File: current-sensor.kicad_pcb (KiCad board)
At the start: 2 copper layers, 78 x 39.3 mm, 34 parts, among them J1 ‎0197134001‎, J2 ‎0197134001‎, J3 0731000105, J4 Molex_SL_01x02_Male, J5 Molex_SL_01x02_Male, SW1 PN12Sxxx03QE, SW2 OS103011MA7QP1, SW3 OS103011MA7QP1, U1 ACS730xLCTR-20AB, U2 AD8616xRM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

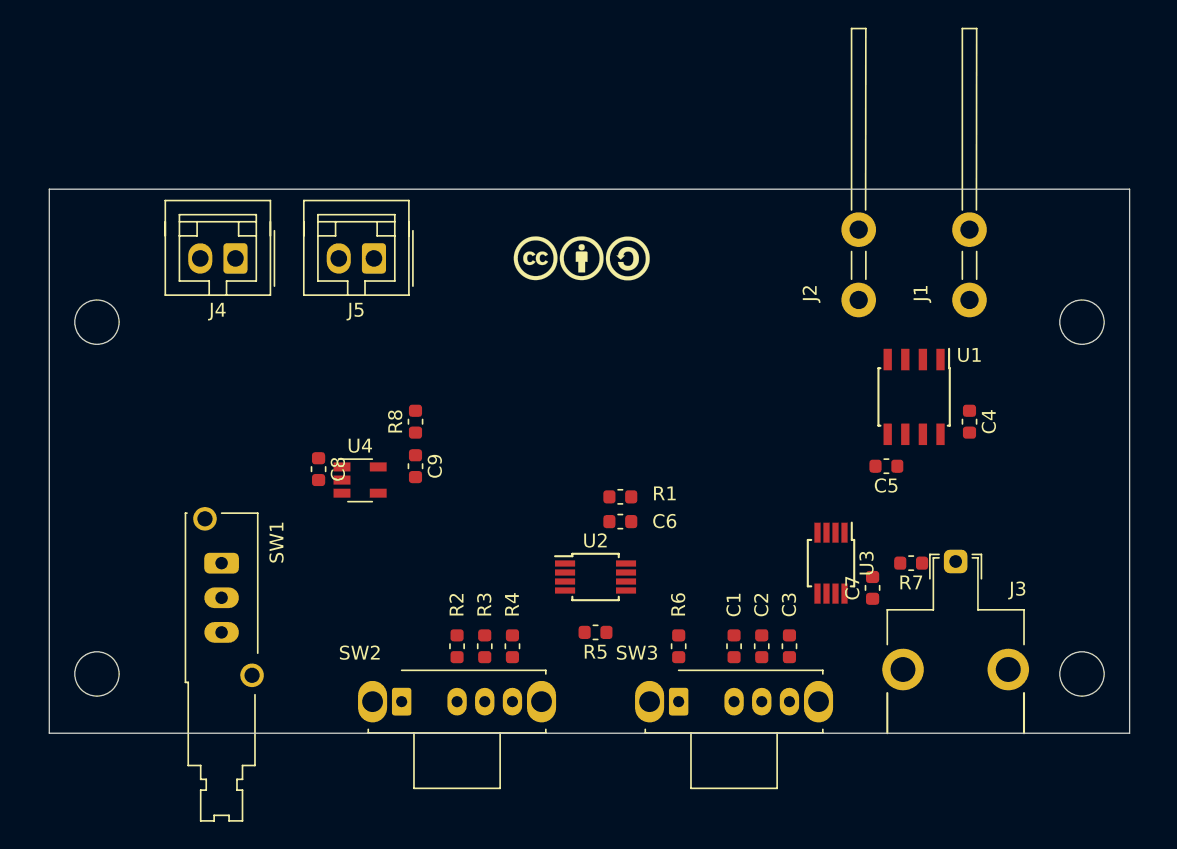
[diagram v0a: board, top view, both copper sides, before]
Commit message: complete mechanical placement of all components on main pcb, and holes on front/back panels
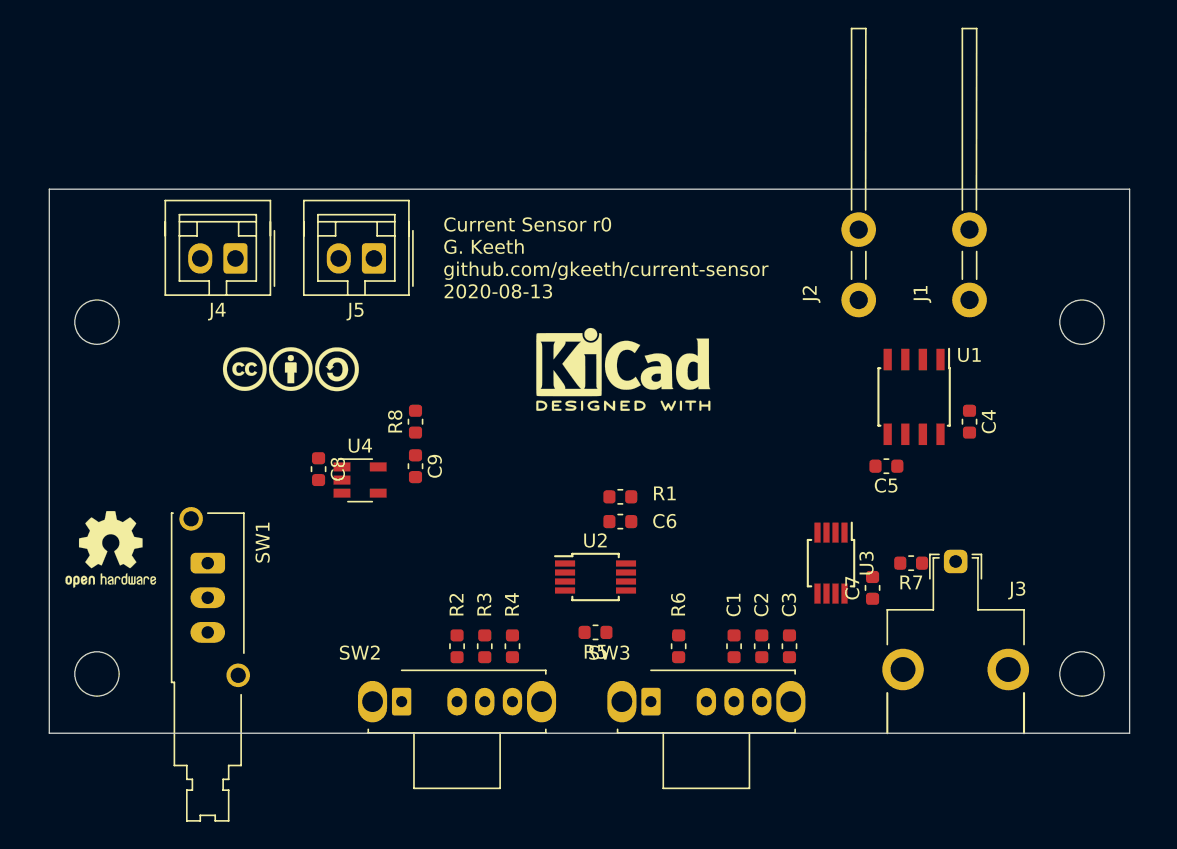
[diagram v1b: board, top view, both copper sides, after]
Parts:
- added LOGO2: Logo_MadeWithKiCad, Symbol:KiCad-Logo2_6mm_SilkScreen, F.Cu at (138.0, 78.0)
- added LOGO3: Logo_Open_Hardware_Small, Symbol:OSHW-Logo2_7.3x6mm_SilkScreen, F.Cu at (101.0, 91.0)
- U1: value ACS730xLCTR-20AB -> ACS730xLCTR-40AB
- moved LOGO1 22.5 mm to (114.0, 78.0)
- moved SW3 2.00 mm to (140.0, 102.0)
- moved SW1 1.00 mm to (108.0, 92.0)
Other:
- board text added: "Current Sensor r0 G. Keeth github.com/gkeeth/current-sensor 2020-08-13"

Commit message: complete basic schematic & routing
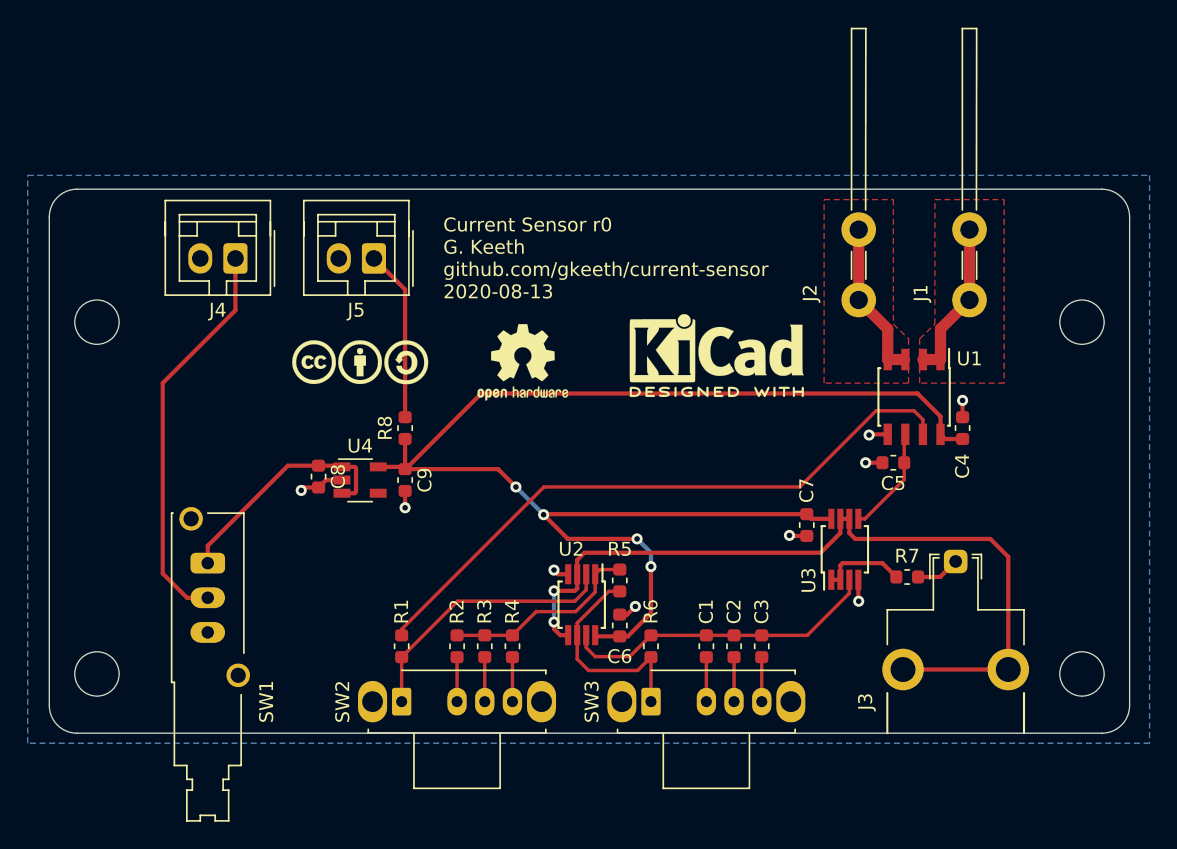
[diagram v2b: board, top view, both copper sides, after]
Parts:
- SW1: value PN12Sxxx03QE -> PN12SHNA03QE
- moved LOGO3 32.7 mm to (130.8, 77.5)
- moved R1 19.1 mm to (122.0, 98.0), turned to 270 degrees
- moved C6 7.50 mm to (137.8, 96.5), turned to 90 degrees
- moved LOGO2 6.82 mm to (144.8, 77.0)
- moved C7 6.57 mm to (151.2, 89.2), turned to 270 degrees
- moved LOGO1 5.02 mm to (119.0, 77.5)
- moved R5 4.14 mm to (137.8, 93.2), turned to 90 degrees
- moved U2 2.24 mm to (135.0, 95.0), turned to 270 degrees
- moved C1 2.00 mm to (144.0, 98.0)
- moved C2 2.00 mm to (146.0, 98.0)
- moved C3 2.00 mm to (148.0, 98.0)
- moved R6 2.00 mm to (140.0, 98.0)
- moved U3 1.41 mm to (154.0, 91.0), turned to 90 degrees
- moved C9 1.25 mm to (122.2, 86.0)
- moved R7 1.04 mm to (158.5, 93.0)
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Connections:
- net Net-(C8-Pad1) renamed /9V_switched
- net Net-(J1-Pad1) renamed /current+
- net Net-(J2-Pad1) renamed /current-
- net Net-(J3-Pad1) renamed /vout
- net Net-(J3-Pad2) renamed /virtual_gnd
- net Net-(J4-Pad1) renamed /9V
- net Net-(J5-Pad1) renamed /led_high
- R6 pad 1: Net-(C1-Pad1) -> Net-(R5-Pad1)
- R6 pad 2: Net-(R5-Pad1) -> Net-(C1-Pad1)
- SW2 pad 1: Net-(R1-Pad1) -> Net-(R1-Pad2)
- U1 pad 7: Net-(R1-Pad2) -> Net-(R1-Pad1)
- U2 pad 2: Net-(R1-Pad1) -> Net-(R1-Pad2)
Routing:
- net +5V: track 0.00 -> 99.2 mm, vias 0 -> 4
- net /virtual_gnd: track 0.00 -> 58.2 mm, vias 0 -> 2
- net Net-(R1-Pad1): track 0.00 -> 45.9 mm
- net /9V: track 0.00 -> 28.9 mm
- net Net-(C1-Pad1): track 0.00 -> 23.0 mm
- net Net-(R1-Pad2): track 0.00 -> 19.7 mm
- net /9V_switched: track 0.00 -> 17.2 mm
- net Net-(R5-Pad1): track 0.00 -> 15.9 mm
- net Net-(R2-Pad1): track 0.00 -> 14.5 mm
- net GND: track 0.00 -> 13.6 mm, vias 0 -> 9
- net /led_high: track 0.00 -> 12.4 mm
- net /current+: track 0.00 -> 11.5 mm
- net /current-: track 0.00 -> 11.5 mm
- net Net-(C5-Pad1): track 0.00 -> 7.78 mm
- net Net-(R7-Pad2): track 0.00 -> 6.20 mm
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- added copper zone on F.Cu, net /current+
- added copper zone on F.Cu, net /current-
- added copper zone on B.Cu, net GND
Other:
- outline, holes or cut-outs redrawn
- net class analog added: clearance 0.2, trace_width 0.25, via_dia 0.8, via_drill 0.4
- net class high_current added: clearance 0.508, trace_width 0.8128, via_dia 1.6, via_drill 0.4
- net class output added: clearance 0.2, trace_width 0.3048, via_dia 0.8, via_drill 0.4
- net class power added: clearance 0.2, trace_width 0.3048, via_dia 0.8, via_drill 0.4
